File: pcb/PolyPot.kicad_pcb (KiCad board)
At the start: 2 copper layers, 30 parts, among them J1 V_BAT_1S, J2 PROG/DEBUG, J3 ANALOG_CONN, J4 TOF_DIST_SENS, M1 DC_WATER_PUMP, Q1 Q_NMOS_DGS, Q2 PMV250EPEAR, SW1 PROG, SW2 RESET, U1 MCP1703A-3002_SOT89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

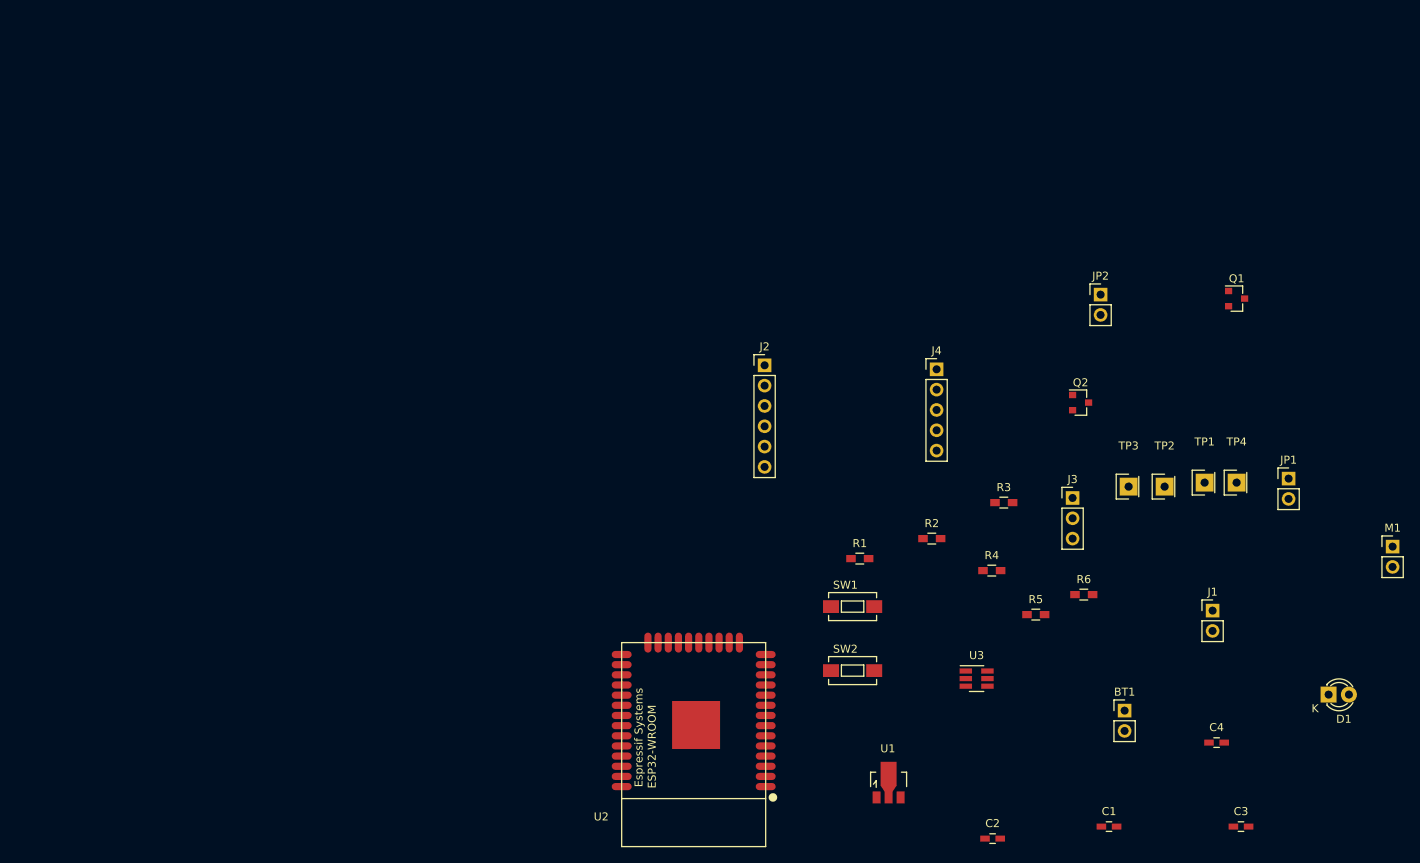
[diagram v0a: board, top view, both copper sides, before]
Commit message: Add ESP32 3d shape
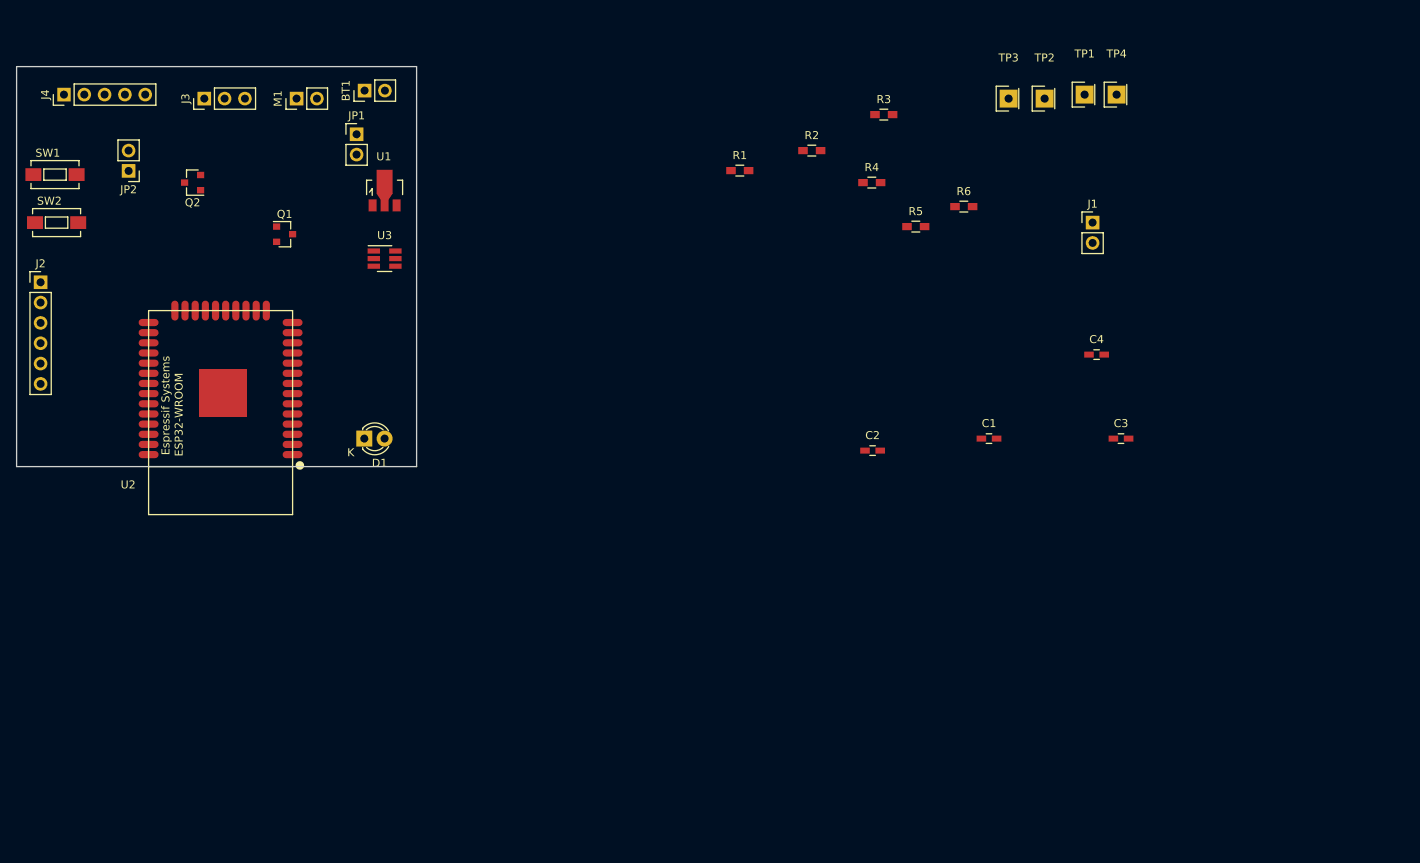
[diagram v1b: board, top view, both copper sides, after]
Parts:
- moved M1 148.0 mm to (65.0, 34.0), turned to 90 degrees
- moved D1 124.7 mm to (73.5, 76.5)
- moved JP1 124.2 mm to (72.5, 38.5)
- moved BT1 122.6 mm to (73.5, 33.0), turned to 90 degrees
- moved JP2 122.5 mm to (44.0, 43.0), turned to 180 degrees
- moved J3 119.5 mm to (53.5, 34.0), turned to 90 degrees
- moved Q1 119.3 mm to (63.5, 51.0)
- moved J4 114.4 mm to (35.9, 33.5), turned to 90 degrees
- moved Q2 114.4 mm to (52.0, 44.5), turned to 180 degrees
- moved SW2 114.2 mm to (35.0, 49.5)
- moved SW1 113.4 mm to (34.8, 43.5)
- moved U1 97.2 mm to (76.0, 45.5)
- moved J2 91.1 mm to (33.0, 57.0)
- moved U3 90.7 mm to (76.0, 54.0)
- moved U2 72.2 mm to (55.5, 73.2)
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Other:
- board outline added: 50 x 50 mm

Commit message: PCB: rough component placement
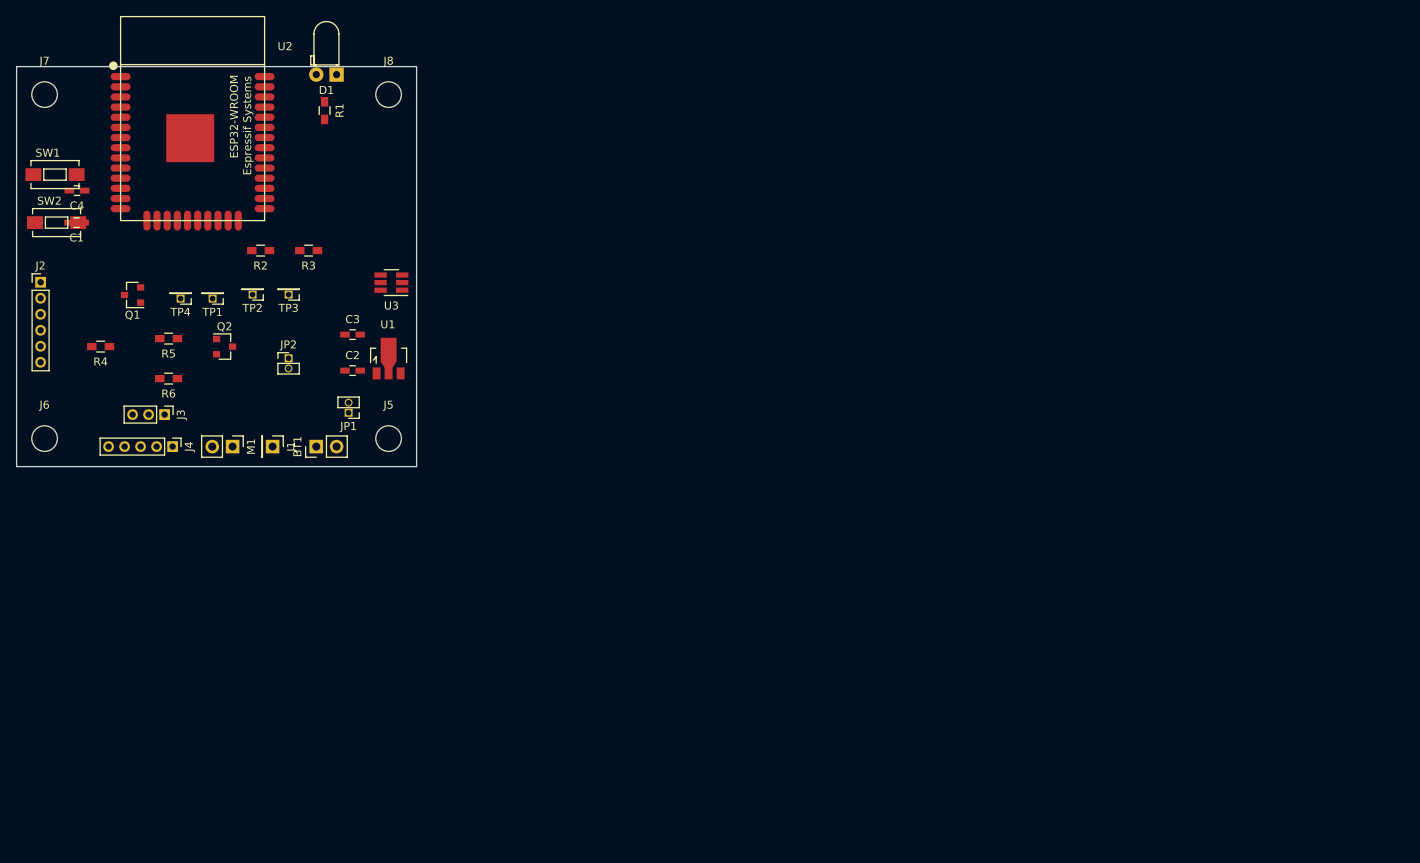
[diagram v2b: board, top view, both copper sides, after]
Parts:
- added J5: M3, Mounting_Holes:MountingHole_3.2mm_M3, F.Cu at (76.5, 76.5)
- added J6: M3, Mounting_Holes:MountingHole_3.2mm_M3, F.Cu at (33.5, 76.5)
- added J7: M3, Mounting_Holes:MountingHole_3.2mm_M3, F.Cu at (33.5, 33.5)
- added J8: M3, Mounting_Holes:MountingHole_3.2mm_M3, F.Cu at (76.5, 33.5)
- D1: footprint LEDs:LED-3MM -> LEDs:LED_D3.0mm_Horizontal_O1.27mm_Z2.0mm
- J1: footprint Socket_Strips:Socket_Strip_Straight_1x02_Pitch2.54mm -> Socket_Strips:Socket_Strip_Straight_1x01_Pitch2.54mm
- J2: footprint Socket_Strips:Socket_Strip_Straight_1x06_Pitch2.54mm -> Socket_Strips:Socket_Strip_Straight_1x06_Pitch2.00mm
- J3: footprint Socket_Strips:Socket_Strip_Straight_1x03_Pitch2.54mm -> Socket_Strips:Socket_Strip_Straight_1x03_Pitch2.00mm
- J4: footprint Socket_Strips:Socket_Strip_Straight_1x05_Pitch2.54mm -> Socket_Strips:Socket_Strip_Straight_1x05_Pitch2.00mm
- JP1, JP2: footprint Socket_Strips:Socket_Strip_Straight_1x02_Pitch2.54mm -> Socket_Strips:Socket_Strip_Straight_1x02_Pitch1.27mm
- TP1, TP2, TP3, TP4: footprint Socket_Strips:Socket_Strip_Straight_1x01 -> Socket_Strips:Socket_Strip_Straight_1x01_Pitch1.27mm
- moved C4 129.1 mm to (37.5, 45.5), turned to 180 degrees
- moved TP4 119.7 mm to (50.5, 59.0), turned to 180 degrees
- moved C1 117.2 mm to (37.5, 49.5), turned to 180 degrees
- moved TP1 111.9 mm to (54.5, 59.0), turned to 180 degrees
- moved J1 106.3 mm to (62.0, 77.5), turned to 270 degrees
- moved TP2 102.0 mm to (59.5, 58.5), turned to 180 degrees
- moved R6 101.7 mm to (49.0, 69.0), turned to 180 degrees
- moved R4 98.6 mm to (40.5, 65.0), turned to 180 degrees
- moved C3 96.9 mm to (72.0, 63.5)
- moved R5 94.4 mm to (49.0, 64.0), turned to 180 degrees
- moved TP3 93.3 mm to (64.0, 58.5), turned to 180 degrees
- moved R3 73.9 mm to (66.5, 53.0), turned to 180 degrees
- moved R2 70.0 mm to (60.5, 53.0), turned to 180 degrees
- moved C2 65.8 mm to (72.0, 68.0)
- moved R1 52.4 mm to (68.5, 35.5), turned to 270 degrees
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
